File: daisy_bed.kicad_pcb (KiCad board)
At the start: 2 copper layers, 79.5 x 101.8 mm, 42 parts, among them J1 EURO_JACK, J10 EURO_JACK, J11 EURO_JACK, J12 EURO_JACK, J13 EURO_JACK, J14 EURO_JACK, J15 EuroPower, J2 EURO_JACK, J3 EURO_JACK, J4 EURO_JACK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

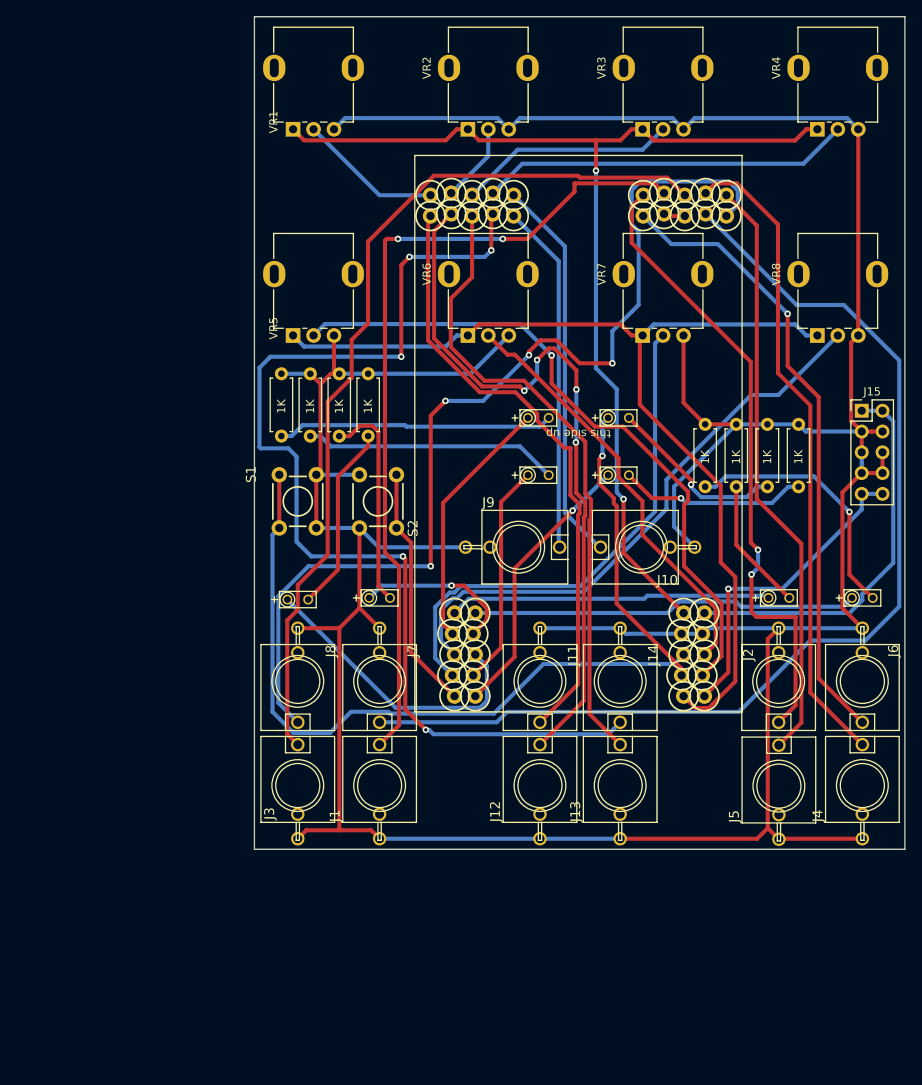
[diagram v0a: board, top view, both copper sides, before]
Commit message: Moves top left corner of PCB to 50,50mm.
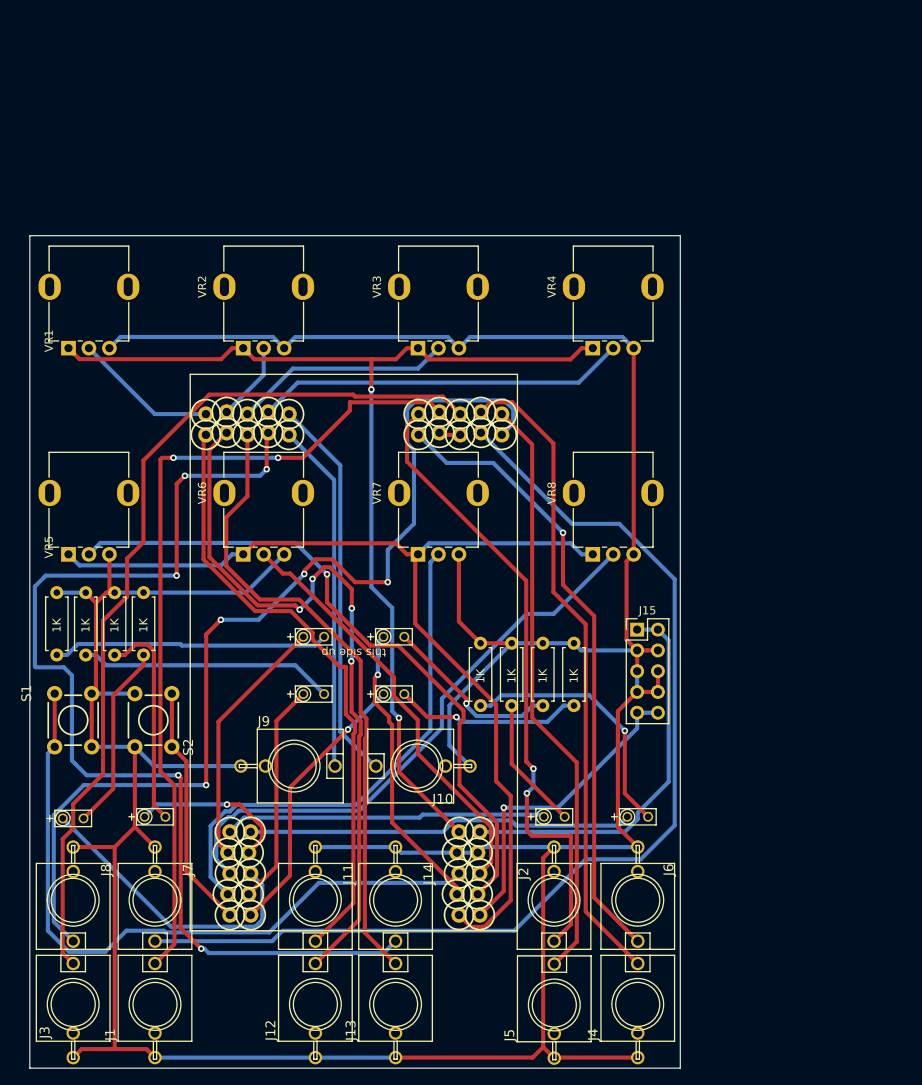
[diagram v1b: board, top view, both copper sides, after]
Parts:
- moved J1 38.3 mm to (65.3, 144.0)
- moved J13 38.3 mm to (94.7, 144.0)
- moved J3 38.3 mm to (55.3, 144.0)
- moved J4 38.3 mm to (124.3, 144.0)
- moved J15 38.3 mm to (124.2, 98.2)
- moved J5 38.3 mm to (114.1, 144.0)
- moved LED3 38.3 mm to (114.1, 121.0)
- moved J10 38.3 mm to (97.3, 114.8)
- moved J12 38.3 mm to (84.9, 144.0)
- moved J14 38.3 mm to (94.7, 131.2)
- moved J6 38.3 mm to (124.3, 131.2)
- moved J7 38.3 mm to (65.3, 131.2)
- moved J8 38.3 mm to (55.3, 131.2)
- moved J9 38.3 mm to (82.3, 114.8)
- moved LED1 38.3 mm to (94.5, 99.0)
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
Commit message: Centres the potentiometers on the board; narrows the PCB to 78.025mm.
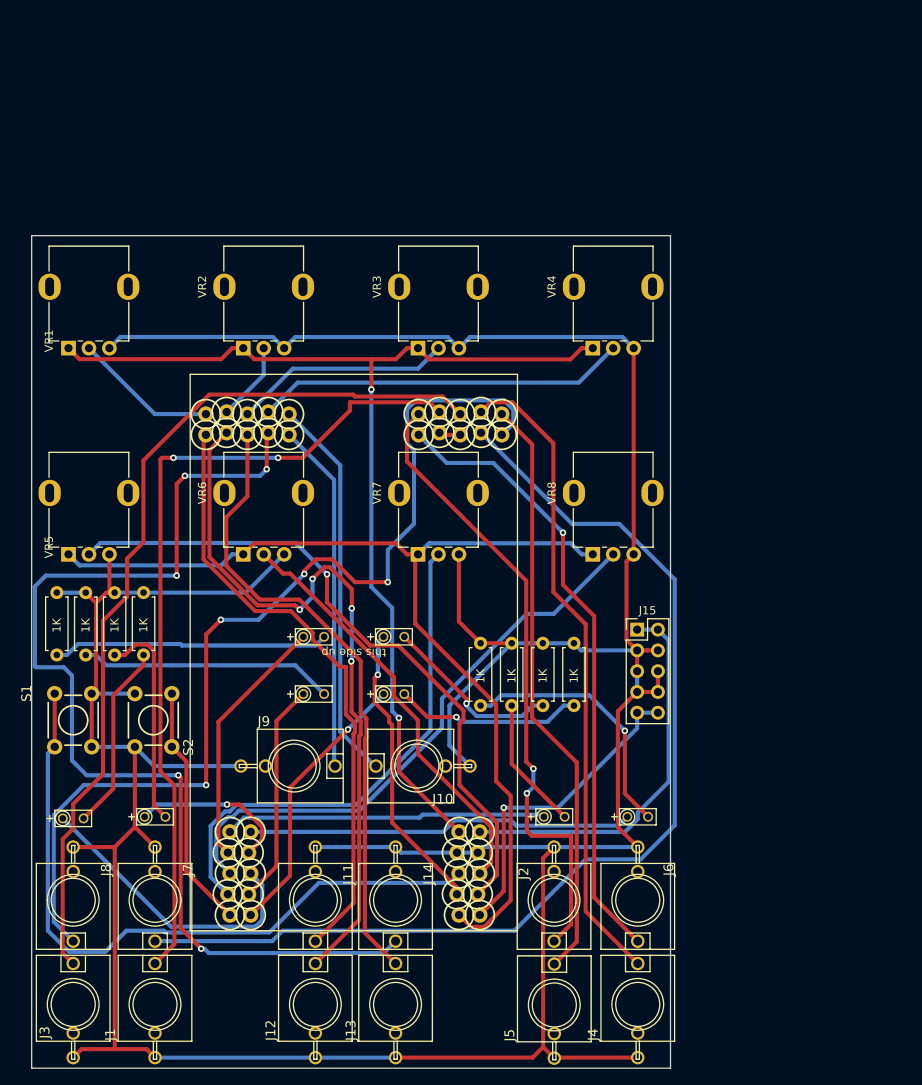
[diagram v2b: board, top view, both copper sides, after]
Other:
- board size 79.5 x 101.8 mm -> 78.1 x 101.8 mm
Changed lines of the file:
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@@
   (gr_line (start 69.1 30.9) (end 69.2 59.4)
     (stroke (width 0.15) (type solid)) (layer "Cmts.User"))
-  (gr_rect (start 50 50) (end 129.5 151.75)
+  (gr_rect (start 50.225 50) (end 128.3 151.75)
     (stroke (width 0.1) (type solid)) (fill none) (layer "Edge.Cuts"))
   (segment (start 83.35 77.15) (end 80.35 77.15) (width 0.5) (layer "F.Cu") (net 1))

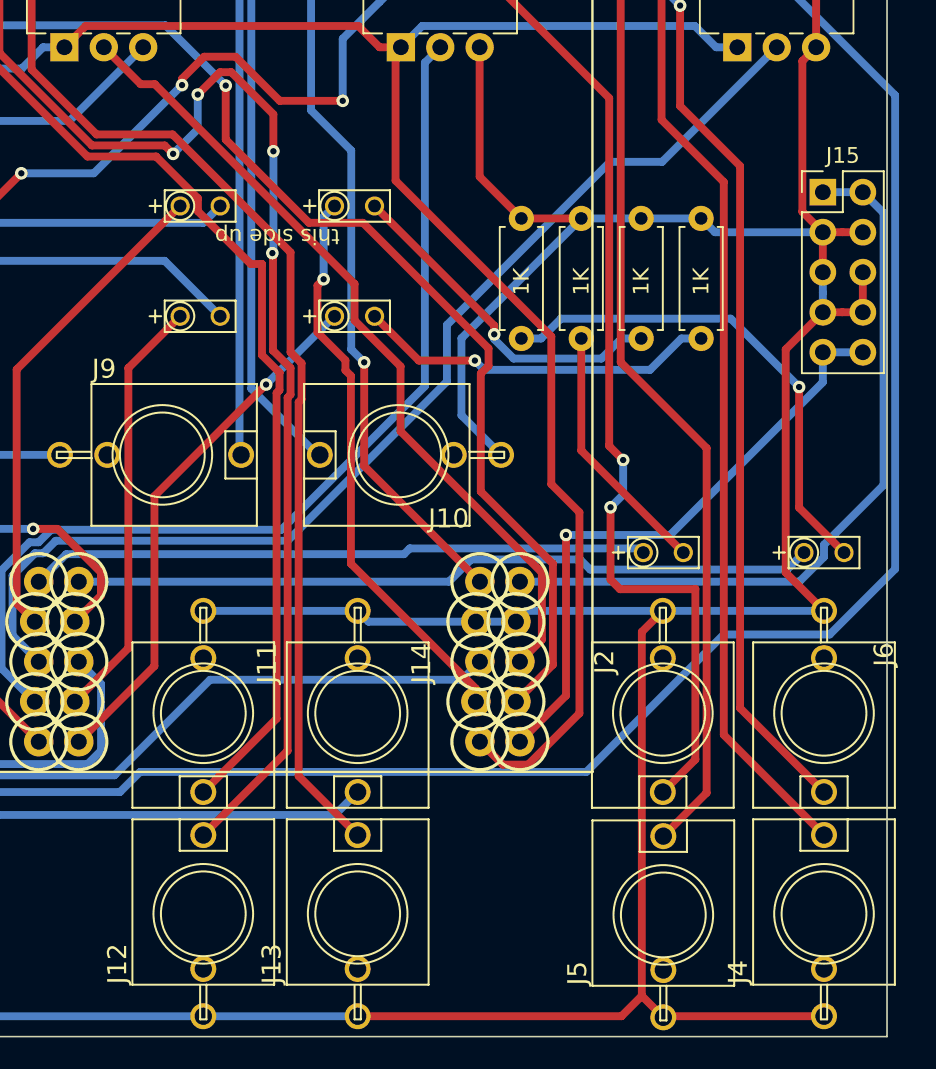
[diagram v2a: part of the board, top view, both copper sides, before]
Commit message: Aligns all jacks.
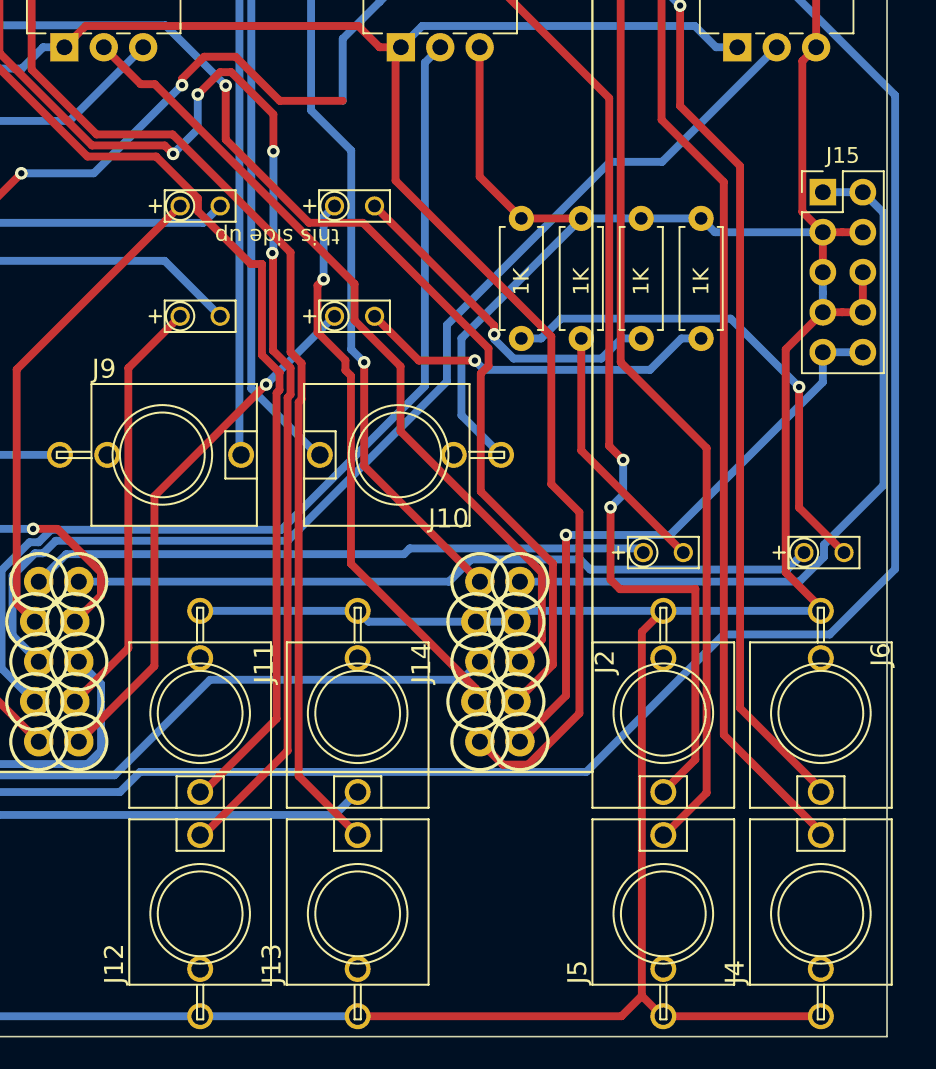
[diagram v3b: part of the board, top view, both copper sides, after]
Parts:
- moved J11 0.20 mm to (84.7, 131.2)
- moved J12 0.20 mm to (84.7, 144.0)
- moved J4 0.20 mm to (124.1, 144.0)
- moved J6 0.20 mm to (124.1, 131.2)
- moved J5 0.07 mm to (114.1, 144.0)
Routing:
- net GATE_IN_1: vias 4 -> 3
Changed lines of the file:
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@@
   )
   (footprint "ES_Daisy_Patch_SM_FB_Rev1:S_JACK" (layer "F.Cu")
-    (at 84.9 143.9557)
+    (at 84.7 143.9557)
     (property "Sheetfile" "File: daisy_bed.kicad_sch")
     (property "Sheetname" "")
@@
   )
   (footprint "ES_Daisy_Patch_SM_FB_Rev1:S_JACK" (layer "F.Cu")
-    (at 124.3 131.225 180)
+    (at 124.1 131.225 180)
     (property "Sheetfile" "File: daisy_bed.kicad_sch")
     (property "Sheetname" "")
@@
   )
   (footprint "ES_Daisy_Patch_SM_FB_Rev1:S_JACK" (layer "F.Cu")
-    (at 114.0693 131.225 180)
+    (at 114.1 131.225 180)
     (property "Sheetfile" "File: daisy_bed.kicad_sch")
     (property "Sheetname" "")
@@
   )
   (footprint "ES_Daisy_Patch_SM_FB_Rev1:S_JACK" (layer "F.Cu")
-    (at 84.9 131.225 180)
+    (at 84.7 131.225 180)
     (property "Sheetfile" "File: daisy_bed.kicad_sch")
     (property "Sheetname" "")
@@
   )
   (footprint "ES_Daisy_Patch_SM_FB_Rev1:S_JACK" (layer "F.Cu")
-    (at 114.1 144.025)
+    (at 114.1 143.956)
     (property "Sheetfile" "File: daisy_bed.kicad_sch")
     (property "Sheetname" "")
@@
   )
   (footprint "ES_Daisy_Patch_SM_FB_Rev1:S_JACK" (layer "F.Cu")
-    (at 124.3 143.9557)
+    (at 124.1 143.9557)
     (property "Sheetfile" "File: daisy_bed.kicad_sch")
     (property "Sheetname" "")
@@
       (net 35 "Net-(LED2-PadK)") (pinfunction "C") (pintype "passive") (solder_mask_margin 0.0762))
   )
-  (gr_line (start 111.8 30.9) (end 111.8 59.5)
-    (stroke (width 0.15) (type solid)) (layer "Cmts.User"))
-  (gr_line (start 136.2 99.2) (end 137.8 99.2)
-    (stroke (width 0.15) (type solid)) (layer "Cmts.User"))
-  (gr_line (start 106.4 84.2) (end 106.4 85.5)
-    (stroke (width 0.15) (type solid)) (layer "Cmts.User"))
-  (gr_line (start 64.2 59.4) (end 137.9 59.6)
-    (stroke (width 0.15) (type solid)) (layer "Cmts.User"))
-  (gr_line (start 136.2 103.5) (end 136.2 129.3)
-    (stroke (width 0.15) (type solid)) (layer "Cmts.User"))
-  (gr_line (start 67.2 87.4) (end 67.2 89.2)
-    (stroke (width 0.15) (type solid)) (layer "Cmts.User"))
-  (gr_line (start 137.5 122.1) (end 67.2 122.1)
-    (stroke (width 0.15) (type solid)) (layer "Cmts.User"))
-  (gr_line (start 126 99.2) (end 127.4 99.2)
-    (stroke (width 0.15) (type solid)) (layer "Cmts.User"))
-  (gr_line (start 106.4 77.2) (end 106.4 78.7)
-    (stroke (width 0.15) (type solid)) (layer "Cmts.User"))
-  (gr_line (start 67.2 87.4) (end 77 87.4)
-    (stroke (width 0.15) (type solid)) (layer "Cmts.User"))
-  (gr_line (start 126 99.2) (end 126.1 96.7)
-    (stroke (width 0.15) (type solid)) (layer "Cmts.User"))
-  (gr_line (start 67.2 99.4) (end 67.2 97.7)
-    (stroke (width 0.15) (type solid)) (layer "Cmts.User"))
-  (gr_line (start 126 103.3) (end 126 129.3)
-    (stroke (width 0.15) (type solid)) (layer "Cmts.User"))
-  (gr_line (start 137.5 109.4) (end 67.2 109.4)
-    (stroke (width 0.15) (type solid)) (layer "Cmts.User"))
-  (gr_line (start 109.3 91.8) (end 109.3 93)
-    (stroke (width 0.15) (type solid)) (layer "Cmts.User"))
-  (gr_line (start 96.6 77.2) (end 96.7 79.3)
-    (stroke (width 0.15) (type solid)) (layer "Cmts.User"))
-  (gr_line (start 106.6 103.5) (end 106.6 126.1)
-    (stroke (width 0.15) (type solid)) (layer "Cmts.User"))
-  (gr_line (start 77.2 99.2) (end 75.9 99.1)
-    (stroke (width 0.15) (type solid)) (layer "Cmts.User"))
-  (gr_line (start 133.2 30.9) (end 133.2 59.4)
-    (stroke (width 0.15) (type solid)) (layer "Cmts.User"))
-  (gr_line (start 67.2 99.4) (end 65.9 99.4)
-    (stroke (width 0.15) (type solid)) (layer "Cmts.User"))
-  (gr_line (start 77.2 99.2) (end 77.2 98.1)
-    (stroke (width 0.15) (type solid)) (layer "Cmts.User"))
-  (gr_line (start 67.2 103.3) (end 67.2 126.3)
-    (stroke (width 0.15) (type solid)) (layer "Cmts.User"))
-  (gr_line (start 96.6 77.2) (end 98.2 77.2)
-    (stroke (width 0.15) (type solid)) (layer "Cmts.User"))
-  (gr_line (start 136.2 99.2) (end 136.3 96.5)
-    (stroke (width 0.15) (type solid)) (layer "Cmts.User"))
-  (gr_line (start 96.6 84.2) (end 96.5 85.4)
-    (stroke (width 0.15) (type solid)) (layer "Cmts.User"))
-  (gr_line (start 94.2 91.7) (end 94.2 93)
-    (stroke (width 0.15) (type solid)) (layer "Cmts.User"))
-  (gr_line (start 106.4 77.2) (end 104.7 77.2)
-    (stroke (width 0.15) (type solid)) (layer "Cmts.User"))
-  (gr_line (start 64.2 34.4) (end 137.8 34.4)
-    (stroke (width 0.15) (type solid)) (layer "Cmts.User"))
-  (gr_line (start 96.8 103.3) (end 96.8 126.1)
-    (stroke (width 0.15) (type solid)) (layer "Cmts.User"))
-  (gr_line (start 77 87.4) (end 77 89.4)
-    (stroke (width 0.15) (type solid)) (layer "Cmts.User"))
-  (gr_line (start 106.4 84.2) (end 105 84.2)
-    (stroke (width 0.15) (type solid)) (layer "Cmts.User"))
-  (gr_line (start 96.6 84.2) (end 95.4 84.1)
-    (stroke (width 0.15) (type solid)) (layer "Cmts.User"))
-  (gr_line (start 87.6 93) (end 115.8 93)
-    (stroke (width 0.15) (type solid)) (layer "Cmts.User"))
-  (gr_line (start 90.4 30.9) (end 90.4 59.5)
-    (stroke (width 0.15) (type solid)) (layer "Cmts.User"))
-  (gr_line (start 77.2 103.5) (end 77.2 126.1)
-    (stroke (width 0.15) (type solid)) (layer "Cmts.User"))
-  (gr_line (start 69.1 30.9) (end 69.2 59.4)
-    (stroke (width 0.15) (type solid)) (layer "Cmts.User"))
   (gr_rect (start 50.225 50) (end 128.3 151.75)
     (stroke (width 0.1) (type solid)) (fill none) (layer "Edge.Cuts"))
@@
   (via (at 83.55 91.35) (size 0.8) (drill 0.4) (layers "F.Cu" "B.Cu") (net 16))
   (via (at 73.35 96.95) (size 0.8) (drill 0.4) (layers "F.Cu" "B.Cu") (net 16))
-  (via (at 93.75 92.35) (size 0.8) (drill 0.4) (layers "F.Cu" "B.Cu") (net 16))
   (via (at 71.55 117.15) (size 0.8) (drill 0.4) (layers "F.Cu" "B.Cu") (net 16))
   (segment (start 93.75 88.4119) (end 93.75 92.35) (width 0.5) (layer "B.Cu") (net 16))
